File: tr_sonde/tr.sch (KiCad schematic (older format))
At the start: 96 parts, among them J1 SMA, J2 SMA, J3 SMA, K1 SMDHDR, K2 SMDHDR, K3 SMDHDR, Q1 PBSS4250X, Q2 MMBT2222A, Q3 STD2NK90ZT4, Q4 STD2NK90ZT4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

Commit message: simplified hptr pin diode biasing.. using a sn75372 might be fun for the next redesign
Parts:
- removed C31: 22uF, smd_capacitors:c_1210, symbol CAPAPOL
- removed Q1: PBSS4250X, Transistors_SMD:sot89, symbol NPN_E1
- removed Q2: MMBT2222A, SMD_Packages:SOT23EBC, symbol NPN
- removed R19: 10k, smd_capacitors:c_0805, symbol R
- removed R29: 1k, smd_capacitors:c_0805, symbol R
- removed R30: 150, SMD_Packages:SMD-1210, symbol R
- removed R31, R5, R8: 22, smd_capacitors:c_0805, symbol R
- removed R6, R7: 150, smd_capacitors:c_1210, symbol R
- added C10, C14: 10nF, smd_capacitors:c_0805, symbol C
- C8, R22, R25: footprint SMD_Packages:SMD-1210 -> smd_capacitors:c_1210
- D6, D7, D8, D9: footprint smb_diode:SMB_DO2144AA -> SMD_Packages:DO-214-AA_SMB
- F1: value PTC FUSE (0ZCJ0010FF2E) -> PTC FUSE (1A TRIP); footprint Fuse_Holders_and_Fuses:Fuse_SMD1206_HandSoldering -> smd_capacitors:c_1812
- R14: footprint SMD_Packages:SM1210 -> SMD_Packages:SMD-1206_Pol
- R4: value 1k -> 150; footprint smd_capacitors:c_0805 -> smd_capacitors:c_1210
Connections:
- wire segments 231 -> 214
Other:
- note added: "NOTE:\nheader pinout is mirrored compared to control board\n"
- moved on the sheet: R13

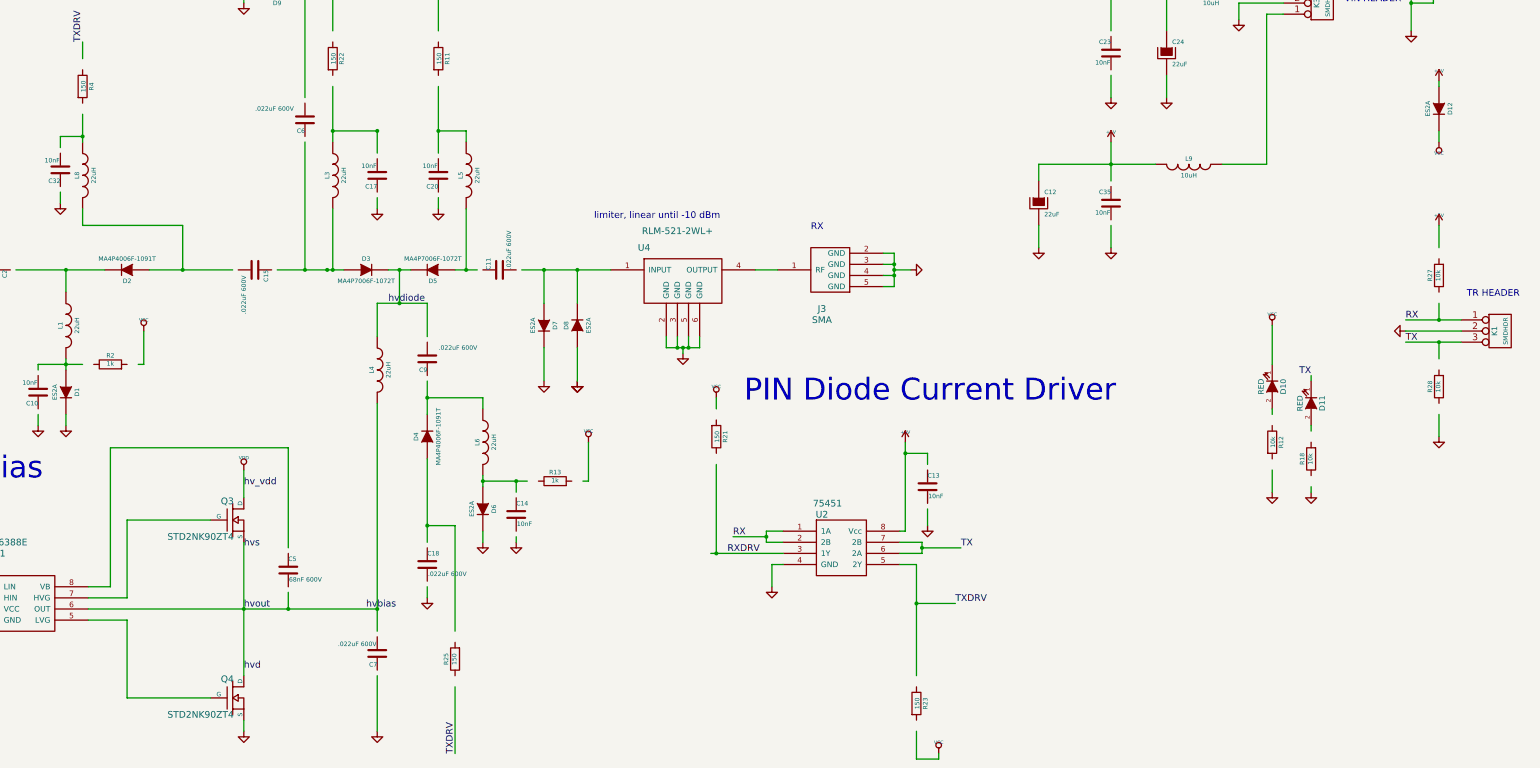
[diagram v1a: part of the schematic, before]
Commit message: added digikey bom for driver amplifier production run
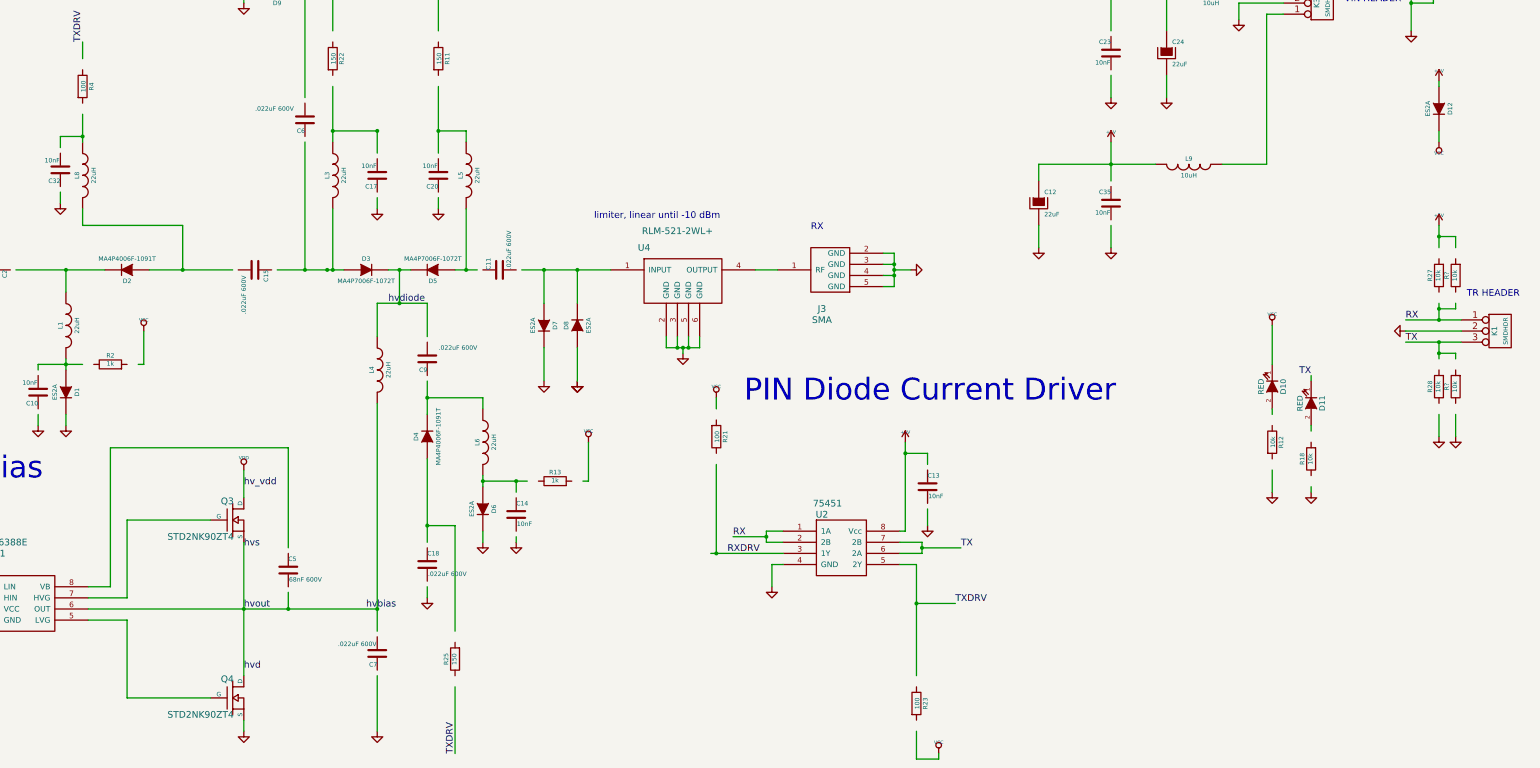
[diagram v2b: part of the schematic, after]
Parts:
- added R? (x2): 10k, smd_capacitors:c_0805, symbol R
- R21, R23, R4: value 150 -> 100
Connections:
- wire segments 214 -> 221
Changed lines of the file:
@@
 	13250 3300 13250 3650
-Wire Wire Line
-	15700 5400 15700 5600
 Wire Wire Line
 	13250 4050 13250 4250
@@
 P 9200 7300
 F 0 "R21" V 9280 7300 40  0000 C CNN
-F 1 "150" V 9207 7301 40  0000 C CNN
+F 1 "100" V 9207 7301 40  0000 C CNN
 F 2 "smd_capacitors:c_1210" V 9130 7300 30  0001 C CNN
 F 3 "~" H 9200 7300 30  0000 C CNN
@@
 P 11000 9700
 F 0 "R23" V 11080 9700 40  0000 C CNN
-F 1 "150" V 11007 9701 40  0000 C CNN
+F 1 "100" V 11007 9701 40  0000 C CNN
 F 2 "smd_capacitors:c_1210" V 10930 9700 30  0001 C CNN
 F 3 "~" H 11000 9700 30  0000 C CNN
@@
 P 3500 4150
 F 0 "R4" V 3580 4150 40  0000 C CNN
-F 1 "150" V 3507 4151 40  0000 C CNN
+F 1 "100" V 3507 4151 40  0000 C CNN
 F 2 "smd_capacitors:c_1210" V 3430 4150 30  0001 C CNN
 F 3 "~" H 3500 4150 30  0000 C CNN
@@
 Wire Wire Line
 	7400 8250 7400 8200
+$Comp
+L R R?
+U 1 1 54FDD5A1
+P 15850 6850
+F 0 "R?" V 15930 6850 40  0000 C CNN
+F 1 "10k" V 15857 6851 40  0000 C CNN
+F 2 "smd_capacitors:c_0805" V 15780 6850 30  0001 C CNN
+F 3 "~" H 15850 6850 30  0000 C CNN
+	1    15850 6850
+	-1   0    0    1
+$EndComp
+Wire Wire Line
+	15850 6600 15850 6550
+Wire Wire Line
+	15850 6550 15700 6550
+Connection ~ 15700 6550
+$Comp
+L GND #PWR?
+U 1 1 54FDD6C1
+P 15850 7300
+F 0 "#PWR?" H 15850 7300 30  0001 C CNN
+F 1 "GND" H 15850 7230 30  0001 C CNN
+F 2 "" H 15850 7300 60  0000 C CNN
+F 3 "" H 15850 7300 60  0000 C CNN
+	1    15850 7300
+	1    0    0    -1
+$EndComp
+Wire Wire Line
+	15850 7300 15850 7100
+Connection ~ 15700 5500
+Wire Wire Line
+	15700 5400 15700 5600
+Wire Wire Line
+	15850 5500 15700 5500
+Wire Wire Line
+	15850 5600 15850 5500
+Wire Wire Line
+	15850 6100 15850 6150
+Connection ~ 15700 6150
+Wire Wire Line
+	15850 6150 15700 6150
+$Comp
+L R R?
+U 1 1 54FDD7E3
+P 15850 5850
+F 0 "R?" V 15930 5850 40  0000 C CNN
+F 1 "10k" V 15857 5851 40  0000 C CNN
+F 2 "smd_capacitors:c_0805" V 15780 5850 30  0001 C CNN
+F 3 "~" H 15850 5850 30  0000 C CNN
+	1    15850 5850
+	-1   0    0    1
+$EndComp
 $EndSCHEMATC

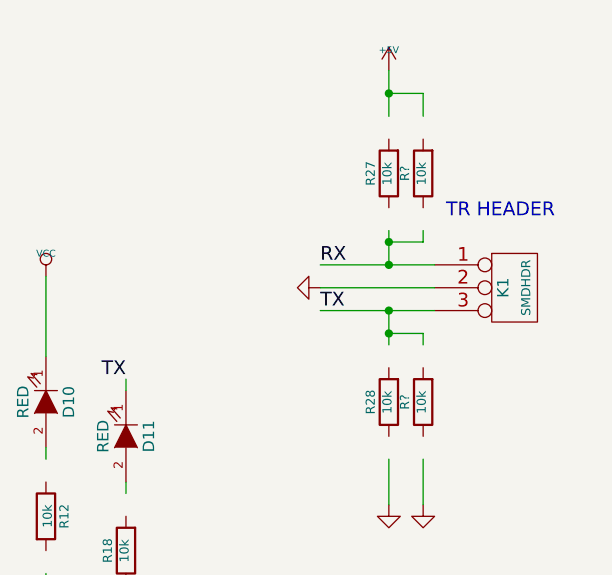
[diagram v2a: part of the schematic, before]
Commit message: added digikey bom for tr
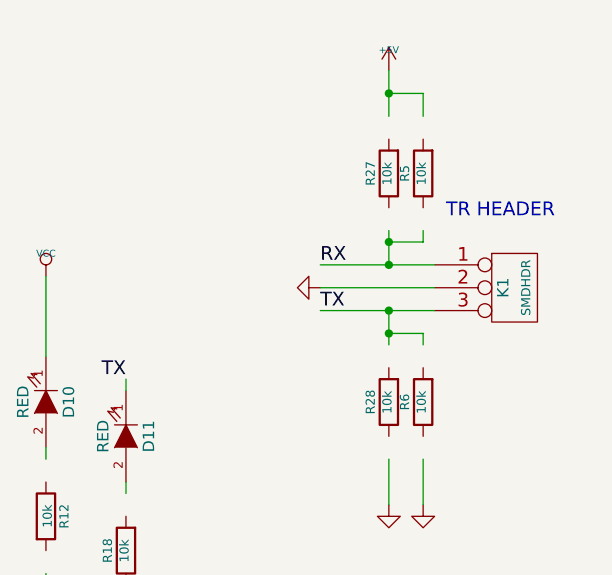
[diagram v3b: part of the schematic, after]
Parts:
- gave numbers to parts that had none: 2

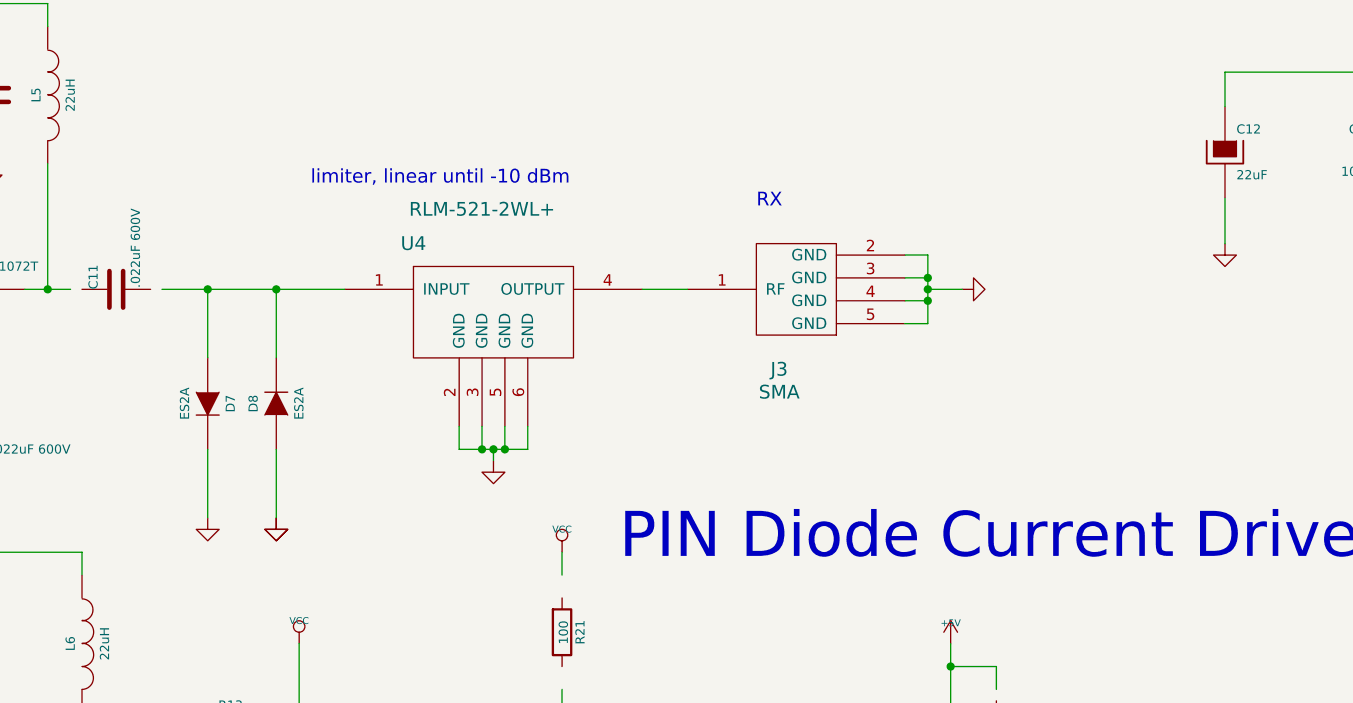
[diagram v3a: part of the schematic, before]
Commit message: updated schematic with distributor part numbers
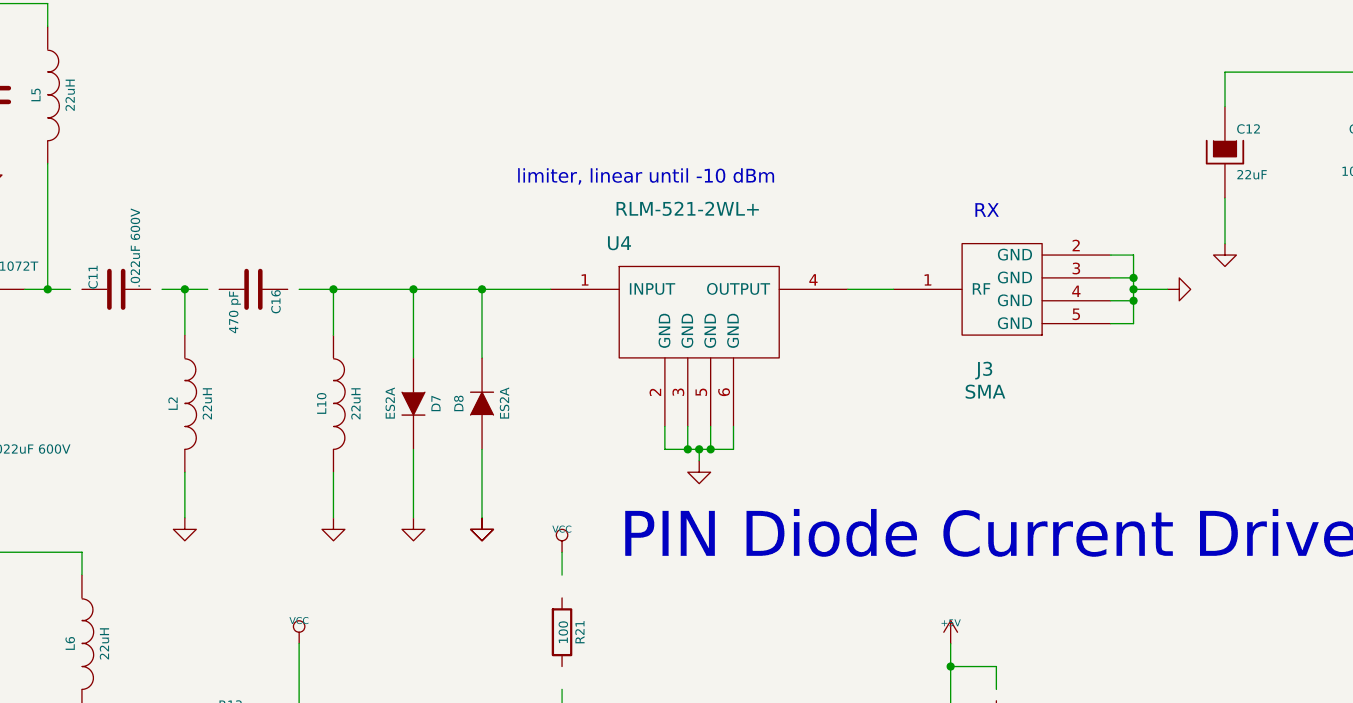
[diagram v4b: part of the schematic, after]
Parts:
- added C16: 470 pF, smd_capacitors:c_0805, symbol C
- added L10, L2: 22uH, smd_capacitors:c_1210, symbol INDUCTOR
- C1, C10, C13, C14, C17, C20, C23, C28, C3, C32, C35, C4: Dist Name (none) -> DigiKey; Dist PN (none) -> 311-1475-6-ND; MFG Name (none) -> YAGEO (VA); MFG PN (none) -> CC0805KRX7R0BB103
- C11, C15, C2, C34, C6, C7, C8: Dist Name (none) -> DigiKey; Dist PN (none) -> 490-5614-6-ND; MFG Name (none) -> MURATA ELECTRONICS (VA); MFG PN (none) -> GCJ32DR72J223KXJ1L
- C12, C24, C27: Dist Name (none) -> DigiKey; Dist PN (none) -> 445-3955-6-ND; MFG Name (none) -> TDK CORPORATION (VA); MFG PN (none) -> C3225X7R1C226M250AC
- C18, C9: Dist Name (none) -> DigiKey; MFG Name (none) -> MURATA ELECTRONICS (VA); MFG PN (none) -> GCJ32DR72J223KXJ1L
- C30: Dist Name (none) -> DigiKey; Dist PN (none) -> 445-6842-6-ND; MFG Name (none) -> TDK CORPORATION (VA); MFG PN (none) -> C5750X7T2J474M250KE
- C5: Dist Name (none) -> DigiKey; Dist PN (none) -> 445-6103-6-ND; MFG Name (none) -> TDK CORPORATION (VA); MFG PN (none) -> C3225X7R2J683K200AM
- D1, D12, D6, D7, D8: Dist Name (none) -> DigiKey; Dist PN (none) -> ES2BFSDKR-ND; MFG Name (none) -> FAIRCHILD SEMICONDUCTOR (VA); MFG PN (none) -> ES2B
- D10, D11: Dist Name (none) -> DigiKey; Dist PN (none) -> 475-1278-6-ND; MFG Name (none) -> OSRAM OPTO SEMICONDUCTORS INC(VA); MFG PN (none) -> LS R976-NR-1
- D2, D4: Dist Name (none) -> DigiKey; Dist PN (none) -> 1465-1228-6-ND; MFG Name (none) -> M/A-COM TECHNOLOGY SOLUTIONS (VA); MFG PN (none) -> MA4P4006F-1091T
- D3, D5: Dist Name (none) -> DigiKey; Dist PN (none) -> 1465-1235-6-ND; MFG Name (none) -> M/A-COM TECHNOLOGY SOLUTIONS (VA); MFG PN (none) -> MA4P7006F-1072T
- D9: Dist Name (none) -> DigiKey; Dist PN (none) -> P6SMB550CALFDKR-ND; MFG Name (none) -> LITTELFUSE INC (VA); MFG PN (none) -> P6SMB550CA
- F1: Dist Name (none) -> DigiKey; Dist PN (none) -> 507-1361-6-ND; MFG Name (none) -> BEL FUSE INC (VA); MFG PN (none) -> 0ZCC0050FF2C
- J1, J2, J3: Dist Name (none) -> DigiKey; Dist PN (none) -> WM9461-ND; MFG Name (none) -> MOLEX INC; MFG PN (none) -> 732511290
- K1, K2, K3: Dist Name (none) -> DigiKey; Dist PN (none) -> WM1341-ND; MFG Name (none) -> MOLEX INC; MFG PN (none) -> 15912035
- L1, L3, L4, L5, L6, L8: Dist Name (none) -> DigiKey; Dist PN (none) -> 490-5341-6-ND; MFG Name (none) -> MURATA ELECTRONICS (VA); MFG PN (none) -> LQH32PN220MN0L
- L7, L9: Dist Name (none) -> DigiKey; Dist PN (none) -> 587-2409-6-ND; MFG Name (none) -> TAIYO YUDEN (VA); MFG PN (none) -> NRS5020T100MMGJ
- Q3, Q4: Dist Name (none) -> DigiKey; Dist PN (none) -> 497-4332-6-ND; MFG Name (none) -> STMICROELECTRONICS (VA); MFG PN (none) -> STD2NK90ZT4
- R1, R10, R12, R16, R17, R18, R27, R28, R5, R6, R9: Dist Name (none) -> DigiKey; Dist PN (none) -> P10.0KCDKR-ND; MFG Name (none) -> PANASONIC ELECTRONIC COMPONENTS (VA); MFG PN (none) -> ERJ-6ENF1002V
- R11, R22, R25: Dist Name (none) -> DigiKey; Dist PN (none) -> P150VDKR-ND; MFG Name (none) -> PANASONIC ELECTRONIC COMPONENTS (VA); MFG PN (none) -> ERJ-14YJ151U
- R13, R2: Dist Name (none) -> DigiKey; Dist PN (none) -> P1.00KCDKR-ND; MFG Name (none) -> PANASONIC ELECTRONIC COMPONENTS (VA); MFG PN (none) -> ERJ-6ENF1001V
- R14: Dist Name (none) -> DigiKey; Dist PN (none) -> HVC1206T1005JETDKR-ND; MFG Name (none) -> OHMITE (VA); MFG PN (none) -> HVC1206T1005JET
- R15, R20: Dist PN (none) -> P10.0KCDKR-ND; MFG Name (none) -> PANASONIC ELECTRONIC COMPONENTS (VA); MFG PN (none) -> ERJ-6ENF1002V
- R21, R23, R4: Dist Name (none) -> DigiKey; Dist PN (none) -> P100VDKR-ND; MFG Name (none) -> PANASONIC ELECTRONIC COMPONENTS (VA); MFG PN (none) -> ERJ-14YJ101U
- R3: Dist Name (none) -> DigiKey; Dist PN (none) -> RHM1.00KAIDKR-ND; MFG Name (none) -> ROHM SEMICONDUCTOR (PASSIVE) (VA); MFG PN (none) -> KTR18EZPF1001
- U1: Dist Name (none) -> DigiKey; Dist PN (none) -> 497-6220-6-ND; MFG Name (none) -> STMICROELECTRONICS (VA); MFG PN (none) -> L6388ED013TR
- U2: Dist Name (none) -> DigiKey; Dist PN (none) -> 296-14960-6-ND; MFG Name (none) -> TEXAS INSTRUMENTS (VA); MFG PN (none) -> SN75451BDR
- U3: Dist Name (none) -> Pico Electronics; Dist PN (none) -> 5SA400; MFG Name (none) -> Pico Electronics; MFG PN (none) -> 5SA400
- U4: Dist Name (none) -> MiniCircuits; Dist PN (none) -> RLM-521-2WL+; MFG Name (none) -> MiniCircuits; MFG PN (none) -> RLM-521-2WL+
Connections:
- wire segments 221 -> 226
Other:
- moved on the sheet: D7, D8, J3, U4

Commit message: updated schematics for newest revision of kicad
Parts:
- removed C11: .022uF 600V, smd_capacitors:c_1210, symbol C
- removed L2: 22uH, smd_capacitors:c_1210, symbol INDUCTOR
- C16: Dist PN 490-1611-1-ND -> 445-15329-6-ND; MFG Name MURATA ELECTRONICS (VA) -> TDK Corporation; MFG PN GRM2165C2A471JA01D -> C2012C0G2W471J060AA
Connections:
- wire segments 226 -> 223
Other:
- note added: "TODO: replace with 500ish ohms\n"
- note added: "TODO: replace with 750 ohms..."
- moved on the sheet: C32, L8, R4
